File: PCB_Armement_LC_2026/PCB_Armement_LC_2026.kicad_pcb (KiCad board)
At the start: 2 copper layers, 97.1 x 72.6 mm, 51 parts, among them J1 Screw_Terminal_01x02, J11 Screw_Terminal_01x02, J17 Screw_Terminal_01x02, J2 Conn_01x06, J20 Screw_Terminal_01x02, J3 Screw_Terminal_01x02, J6 Conn_01x06, J7 Conn_01x06, J8 Screw_Terminal_01x02, J9 Conn_01x04, Q1 DMP10H400SK3-13, Q2 DMP10H400SK3-13, SW1 SW_Nidec_CAS-120A1, SW2 SW_Nidec_CAS-120A1, SW4 SW_Nidec_CAS-120A1, SW5 SW_Nidec_CAS-120A1, SW6 SW_Nidec_CAS-120A1, SW7 SW_Nidec_CAS-120A1, SW8 SW_Nidec_CAS-120A1, SW9 SW_Nidec_CAS-120A1, U1 LDO_4v2-MIC5209-4.2YS-TR

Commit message: Améliorations mineures PCB armement
Améliorations de silkscreen, fix de quelques problemes de drc
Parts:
- added  : LOGO, LOGO, F.Cu at (116.2, 118.5)
- added  : LOGO, LOGO, F.Cu at (172.0, 129.5)
- renumbered C8 to C3, C7 to C4, PWR_R1 to R1, PWR_R2 to R2
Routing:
- net 7v4: track 19.4 -> 18.1 mm
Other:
- board text added: "C3"
- board text added: "C4"
- board text added: "DZ1"
- board text added: "DZ2"
- board text added: "R1"
- board text added: "R2"

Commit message: fix and almost finish PCB
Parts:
- removed  : LOGO, LOGO (x2)
- added G***: LOGO, LOGO, B.Cu at (147.9, 163.3)
- DZ1, DZ2: value SZMMSZ4679T1G -> MMSZ4683-TP
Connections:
- SW2 pad 1: Net-(J17-Pin_2) -> Net-(Q2-D)
- SW2 pad 2: Net-(Q2-D) -> Net-(J17-Pin_2)
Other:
- board text added: "Apo BR"
- board text added: "Apo Strato"
- board text added: "Main BR"
- board text added: "Main Strato"
- board text added: "PCB Armement LC 2026 Alexis Giroux"
- board text added: "Power BR"
- board text added: "Shunt Motor"
- board text added: "Switch Strato"
- board text added: "System"
- board text removed: "Apo BR Apo Strato Main BR Main Strato Shunt Motor +/- BR Switch Strato System"
- board text removed: "C"
- board text removed: "R"
- board text removed: "Z"

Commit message: Added logos
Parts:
- removed the G*** at (147.9, 163.3)
- added G***: LOGO, LOGO, B.Cu at (125.8, 87.2)
- added G***: LOGO, LOGO, B.Cu at (113.9, 109.6)

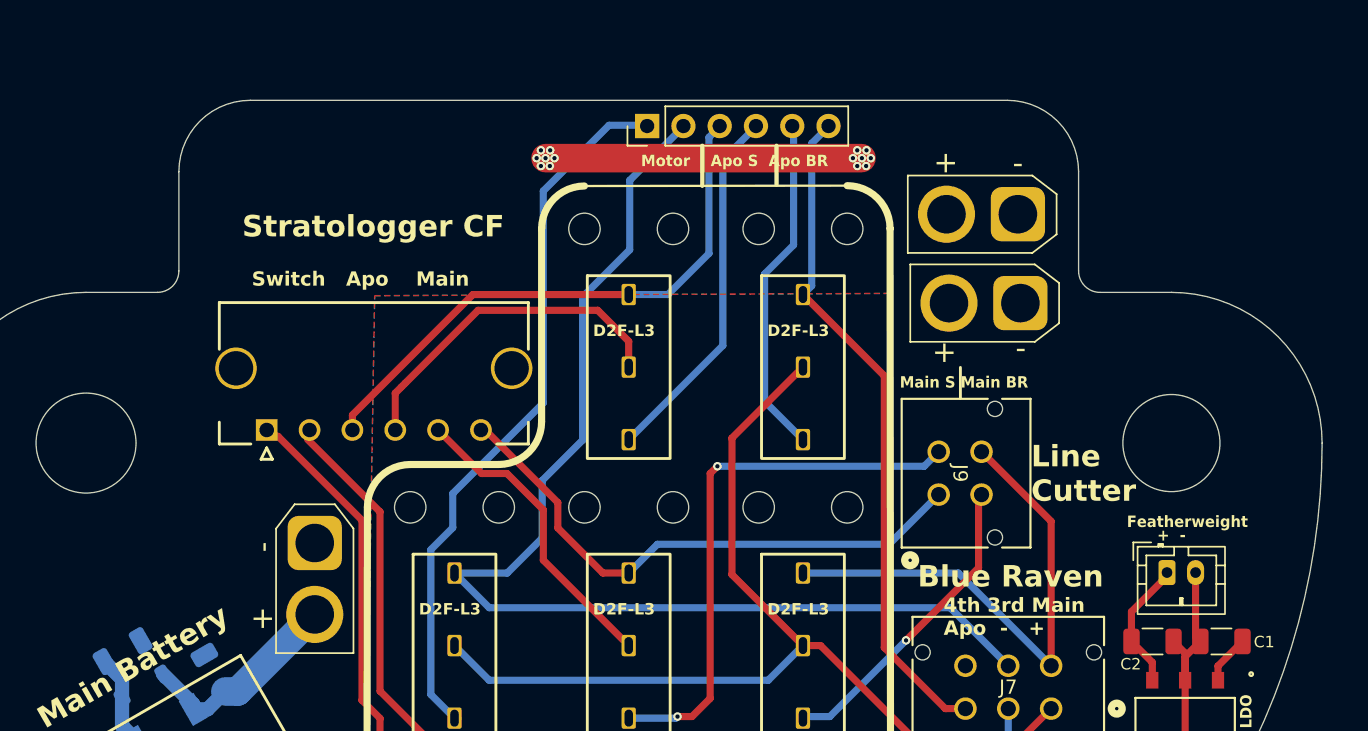
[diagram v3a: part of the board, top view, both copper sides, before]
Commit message: Modif connecteur featherweight strato et terminal block centre
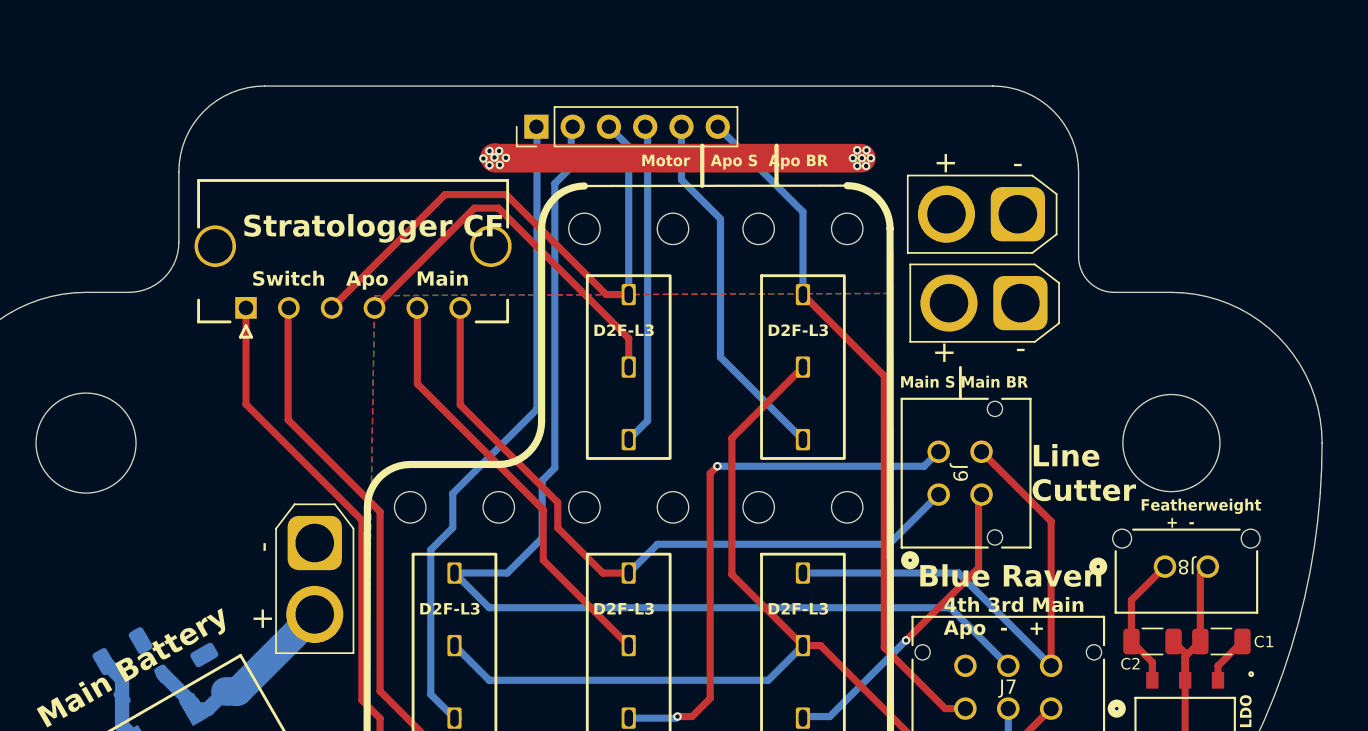
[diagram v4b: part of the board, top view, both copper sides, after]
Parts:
- J8: footprint Connector_JST:JST_PH_B2B-PH-K_1x02_P2.00mm_Vertical -> Library:CONN_4365001002
- moved J6 8.67 mm to (123.2, 92.0)
- moved J2 7.76 mm to (143.5, 79.3)
- moved J8 0.44 mm to (187.6, 110.2), turned to 180 degrees
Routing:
- net Strato S2: track 45.8 -> 55.6 mm
- net Strato S1: track 52.8 -> 62.0 mm
- net Strato Main 2: track 39.5 -> 48.7 mm
- net Strato Main 1: track 21.7 -> 29.8 mm
- net M1: track 50.4 -> 45.5 mm
- net GND: track 42.6 -> 47.2 mm
- net BR1 3rd: track 81.8 -> 78.5 mm
- net Net-(J2-Pin_4): track 25.7 -> 22.5 mm
- net Strato Apo 1: track 24.1 -> 26.5 mm
- net BR1 Apo: track 47.3 -> 48.9 mm
- net Net-(J2-Pin_5): track 24.0 -> 25.4 mm
- net Strato Apo 2: track 40.0 -> 39.3 mm
- net Net-(J8-Pin_1): track 8.93 -> 9.54 mm
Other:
- board size 97.1 x 72.6 mm -> 97.1 x 73.6 mm

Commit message: Send to Fabrication
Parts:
- moved G*** 21.4 mm to (131.9, 98.1)
- moved J2 2.00 mm to (145.5, 79.3)
- moved G*** 1.89 mm to (127.3, 86.2)
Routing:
- net Net-(J2-Pin_4): track 22.5 -> 23.8 mm
- net M1: track 45.5 -> 46.4 mm
- net BR1 3rd: track 78.5 -> 79.3 mm
- net Net-(J2-Pin_5): track 25.4 -> 24.6 mm
- net BR1 Apo: track 48.9 -> 48.3 mm
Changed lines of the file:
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@@
 		(filling no)
 		(pcbplotparams
-			(layerselection 0x00000000_00000000_55555555_5755f5ff)
+			(layerselection 0x00000000_00000000_55555555_575555ff)
 			(plot_on_all_layers_selection 0x00000000_00000000_00000000_00000000)
 			(disableapertmacros no)
@@
 			(outputformat 1)
 			(mirror no)
-			(drillshape 1)
+			(drillshape 0)
 			(scaleselection 1)
-			(outputdirectory "")
+			(outputdirectory "Fab/")
 		)
 	)
@@
 		)
 		(embedded_fonts no)
+		(model "${KIPRJMOD}/step files/436500603.step"
+			(offset
+				(xyz -7.5 -4 2.5)
+			)
+			(scale
+				(xyz 1 1 1)
+			)
+			(rotate
+				(xyz -90 -0 -0)
+			)
+		)
 	)
 	(footprint "MountingHole:MountingHole_2.2mm_M2"
@@
 	(footprint "Connector_PinHeader_2.54mm:PinHeader_1x06_P2.54mm_Vertical"
 		(layer "F.Cu")
-		(at 143.534999 79.349999 90)
+		(at 145.539687 79.349392 90)
 		(descr "Through hole straight pin header, 1x06, 2.54mm pitch, single row")
 		(tags "Through hole pin header THT 1x06 2.54mm single row")
@@
 		(tags "436500227 ")
 		(property "Reference" "J8"
-			(at -1.5 0 180)
+			(at -1.696293 -1.998099 180)
 			(unlocked yes)
 			(layer "F.SilkS")
+			(hide yes)
 			(effects
 				(font
@@
 			)
 		)
-		(property "Datasheet" "https://www.digikey.com/en/products/detail/jst-sales-america-inc/B2B-PH-K-S/926611"
+		(property "Datasheet" "https://www.digikey.com/en/products/detail/molex/0436500215/283461"
 			(at 0 0 0)
 			(layer "F.Fab")
@@
 			)
 		)
-		(property "Digikey_Part_Number" "  455-1704-ND"
+		(property "Digikey_Part_Number" "  WM1917-ND"
 			(at 0 0 180)
 			(unlocked yes)
@@
 			)
 		)
-		(property "Manufacture_Part_Number" "  B2B-PH-K-S"
+		(property "Manufacture_Part_Number" "0436500215"
 			(at 0 0 180)
 			(unlocked yes)
@@
 		(sheetname "/")
 		(sheetfile "PCB_Armement_LC_2026.kicad_sch")
-		(units
-			(unit
-				(name "A")
-				(pins "1" "2")
-			)
-		)
 		(attr through_hole)
 		(duplicate_pad_numbers_are_jumpers no)
@@
 		)
 		(fp_circle
-			(center 4.676399 0.000001)
-			(end 5.057399 0)
+			(center 4.676399 1.7)
+			(end 5.057399 1.699999)
 			(stroke
 				(width 0.508)
@@
 			(layer "F.SilkS")
 		)
-		(fp_circle
-			(center 4.676399 0.000001)
-			(end 5.057399 0)
-			(stroke
-				(width 0.508)
-				(type solid)
-			)
-			(fill no)
-			(layer "B.SilkS")
-		)
 		(fp_line
 			(start 3.914401 2.874401)
@@
 		)
 		(embedded_fonts no)
+		(model "${KIPRJMOD}/step files/436500215.stp"
+			(offset
+				(xyz -1.5 -2 10)
+			)
+			(scale
+				(xyz 1 1 1)
+			)
+			(rotate
+				(xyz 90 -0 -0)
+			)
+		)
 	)
 	(footprint "MountingHole:MountingHole_2.2mm_M2"
@@
 		)
 		(embedded_fonts no)
-		(model "${KICAD10_3DMODEL_DIR}/Connector_AMASS.3dshapes/AMASS_XT30U-F_1x02_P5.0mm_Vertical.step"
+		(model "${KIPRJMOD}/step files/XT30-F_m.ver.STEP"
 			(offset
-				(xyz 0 0 0)
+				(xyz 8 0 0)
 			)
 			(scale
@@
 			)
 			(rotate
-				(xyz 0 0 0)
+				(xyz -0 -0 -90)
 			)
 		)
@@
 	(footprint "LOGO"
 		(layer "B.Cu")
-		(at 125.752645 87.200391 180)
+		(at 127.329734 86.157145 180)
 		(property "Reference" "G***"
 			(at 0 0 0)
@@
 	(footprint "LOGO"
 		(layer "B.Cu")
-		(at 113.863823 109.577554 180)
+		(at 131.880248 98.084388 180)
 		(property "Reference" "G***"
 			(at 0 0 0)
@@
 	)
 	(gr_line
-		(start 155.15 80.679999)
-		(end 155.15 83.488791)
+		(start 149.128909 80.68818)
+		(end 149.128909 83.496972)
 		(stroke
 			(width 0.3)
@@
 	)
 	(gr_line
-		(start 160.35 80.679999)
-		(end 160.35 83.405801)
+		(start 154.080489 80.753443)
+		(end 154.080489 83.479245)
 		(stroke
 			(width 0.3)
@@
 	)
 	(gr_text "Motor    Apo S  Apo BR"
-		(at 150.865215 82.207011 0)
+		(at 144.658929 83.036529 0)
 		(layer "F.SilkS")
 		(effects
@@
 	)
 	(gr_text "Switch   Apo    Main"
-		(at 123.6 90.6 0)
+		(at 121.851514 96.318107 0)
 		(layer "F.SilkS")
 		(effects
@@
 	)
 	(gr_text "Stratologger CF\n\n"
-		(at 122.925 89.625 0)
+		(at 121.416189 101.542014 0)
 		(layer "F.SilkS")
 		(effects
@@
 		)
 	)
+	(gr_text "Motor    Apo S  Apo BR"
+		(at 145.003341 80.97799 180)
+		(layer "B.SilkS")
+		(effects
+			(font
+				(size 0.8 0.75)
+				(thickness 0.1875)
+				(bold yes)
+			)
+			(justify left bottom mirror)
+		)
+	)
 	(gr_text "MOSFET"
 		(at 117.372847 130.278198 300)
@@
 	)
 	(gr_text "PCB Armement LC 2026\nAlexis Giroux"
-		(at 142.287611 83.568433 0)
+		(at 142.389281 82.933015 0)
 		(layer "B.SilkS")
 		(effects
@@
 	)
 	(segment
-		(start 150 80.735)
+		(start 150.619687 79.349392)
+		(end 149.395333 80.573746)
+		(width 0.5)
+		(layer "B.Cu")
+		(net "Strato Apo 2")
+	)
+	(segment
+		(start 149.395333 90.495333)
 		(end 150 91.1)
 		(width 0.5)
@@
 	)
 	(segment
-		(start 148.614999 79.349999)
-		(end 150 80.735)
+		(start 149.395333 80.573746)
+		(end 149.395333 90.495333)
 		(width 0.5)
 		(layer "B.Cu")
@@
 	)
 	(segment
-		(start 143.575 79.39)
-		(end 143.534999 79.349999)
+		(start 143.232755 99.475491)
+		(end 143.232755 81.656324)
 		(width 0.5)
 		(layer "B.Cu")
@@
 	)
 	(segment
-		(start 136.144 119.104)
-		(end 136.144 108.964952)
+		(start 145.975 79.45)
+		(end 146.075 79.35)
 		(width 0.5)
 		(layer "B.Cu")
@@
 	)
 	(segment
-		(start 137.679754 107.429198)
-		(end 137.679754 105.028492)
+		(start 137.8 120.76)
+		(end 136.144 119.104)
 		(width 0.5)
 		(layer "B.Cu")
@@
 	)
 	(segment
-		(start 137.679754 105.028492)
-		(end 143.575 99.133246)
+		(start 143.232755 81.656324)
+		(end 145.539687 79.349392)
 		(width 0.5)
 		(layer "B.Cu")
@@
 	)
 	(segment
-		(start 136.144 108.964952)
-		(end 137.679754 107.429198)
+		(start 137.679754 107.429198)
+		(end 137.679754 105.028492)
 		(width 0.5)
 		(layer "B.Cu")
@@
 	)
 	(segment
-		(start 143.575 99.133246)
-		(end 143.575 79.39)
+		(start 136.144 119.104)
+		(end 136.144 108.964952)
 		(width 0.5)
 		(layer "B.Cu")
@@
 	)
 	(segment
-		(start 137.8 120.76)
-		(end 136.144 119.104)
+		(start 136.144 108.964952)
+		(end 137.679754 107.429198)
 		(width 0.5)
 		(layer "B.Cu")
@@
 	)
 	(segment
-		(start 176.578001 117.094001)
-		(end 172.514 113.03)
-		(width 0.5)
-		(layer "B.Cu")
-		(net "BR1 3rd")
-	)
-	(segment
-		(start 145.975 82.175)
-		(end 145.975 79.45)
+		(start 137.679754 105.028492)
+		(end 143.232755 99.475491)
 		(width 0.5)
 		(layer "B.Cu")
-		(net "BR1 3rd")
+		(net "M1")
 	)
 	(segment
-		(start 141.49672 110.6)
-		(end 143.938737 108.157983)
+		(start 176.578001 117.094001)
+		(end 172.514 113.03)
 		(width 0.5)
 		(layer "B.Cu")
@@
 	)
 	(segment
-		(start 145.975 79.45)
-		(end 146.075 79.35)
+		(start 143.938737 104.128227)
+		(end 144.457108 103.609856)
 		(width 0.5)
 		(layer "B.Cu")
@@
 	)
 	(segment
-		(start 144.825 103.241964)
-		(end 144.825 83.325)
+		(start 148.079688 80.070312)
+		(end 148.079688 79.349393)
 		(width 0.5)
 		(layer "B.Cu")
@@
 	)
 	(segment
-		(start 137.8 110.6)
-		(end 141.49672 110.6)
+		(start 143.938737 108.157983)
+		(end 143.938737 104.128227)
 		(width 0.5)
 		(layer "B.Cu")
@@
 	)
 	(segment
-		(start 144.825 83.325)
-		(end 145.975 82.175)
+		(start 144.457108 103.609856)
+		(end 144.457108 83.692892)
 		(width 0.5)
 		(layer "B.Cu")
@@
 	)
 	(segment
-		(start 143.938737 104.128227)
-		(end 144.825 103.241964)
+		(start 144.457108 83.692892)
+		(end 148.079688 80.070312)
 		(width 0.5)
 		(layer "B.Cu")
@@
 	)
 	(segment
-		(start 143.938737 108.157983)
-		(end 143.938737 104.128227)
+		(start 137.8 110.6)
+		(end 141.49672 110.6)
 		(width 0.5)
 		(layer "B.Cu")
@@
 	)
 	(segment
-		(start 151.325 99.935)
-		(end 151.325 79.52)
+		(start 141.49672 110.6)
+		(end 143.938737 108.157983)
+		(width 0.5)
+		(layer "B.Cu")
+		(net "BR1 3rd")
+	)
+	(segment
+		(start 151.325 89.103407)
+		(end 150.619687 88.398094)
 		(width 0.5)
 		(layer "B.Cu")
@@
 	)
 	(segment
-		(start 151.325 79.52)
-		(end 151.154999 79.349999)
+		(start 151.325 99.935)
+		(end 151.325 89.103407)
 		(width 0.5)
 		(layer "B.Cu")
@@
 	)
 	(segment
-		(start 153.694998 79.35)
-		(end 153.694998 83.069998)
+		(start 150.619687 88.398094)
+		(end 150.619687 81.889392)
 		(width 0.5)
 		(layer "B.Cu")
-		(net "Net-(J2-Pin_5)")
+		(net "Net-(J2-Pin_4)")
 	)
 	(segment
-		(start 156.425 95.485)
-		(end 162.2 101.26)
+		(start 150.619687 81.889392)
+		(end 153.159687 79.349392)
+		(width 0.5)
+		(layer "B.Cu")
+		(net "Net-(J2-Pin_4)")
+	)
+	(segment
+		(start 155.699686 79.349393)
+		(end 156.425 80.074707)
 		(width 0.5)
 		(layer "B.Cu")
@@
 	)
 	(segment
-		(start 156.425 85.8)
+		(start 156.425 80.074707)
 		(end 156.425 95.485)
 		(width 0.5)
@@
 	)
 	(segment
-		(start 153.694998 83.069998)
-		(end 156.425 85.8)
+		(start 156.425 95.485)
+		(end 162.2 101.26)
 		(width 0.5)
 		(layer "B.Cu")
@@
 	)
 	(segment
-		(start 162.2 85.315001)
-		(end 156.234998 79.349999)
+		(start 162.2 91.1)
+		(end 162.2 82.889785)
 		(width 0.5)
 		(layer "B.Cu")
@@
 	)
 	(segment
-		(start 162.2 91.1)
-		(end 162.2 85.315001)
+		(start 162.2 82.889785)
+		(end 158.659607 79.349392)
+		(width 0.5)
+		(layer "B.Cu")
+		(net "BR1 Apo")
+	)
+	(segment
+		(start 158.659607 79.349392)
+		(end 158.239686 79.349392)
 		(width 0.5)
 		(layer "B.Cu")
